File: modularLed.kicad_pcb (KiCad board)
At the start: 2 copper layers, 101.6 x 101.6 mm, 173 parts, among them IC101 ATMEGA328P-A, J101 POWER_JACKPTH, M301 FDS4935BZ, M302 FDS4935BZ, M303 FDS4935BZ, M304 FDS4935BZ, M305 FDS4935BZ, M306 FDS4935BZ, M307 FDS4935BZ, M308 FDS4935BZ, M401 FDS4935BZ, M402 FDS4935BZ, M403 FDS4935BZ, M404 FDS4935BZ, M405 FDS4935BZ, M406 FDS4935BZ, M407 FDS4935BZ, M408 FDS4935BZ, M501 FDS4935BZ, M502 FDS4935BZ, M503 FDS4935BZ, M504 FDS4935BZ, M505 FDS4935BZ, M506 FDS4935BZ, M507 FDS4935BZ, M508 FDS4935BZ, M601 FDS4935BZ, M602 FDS4935BZ, M603 FDS4935BZ, M604 FDS4935BZ, M605 FDS4935BZ, M606 FDS4935BZ, M607 FDS4935BZ, M608 FDS4935BZ, P101 CONN_01X04, P102 CONN_01X04, P103 CONN_01X04, P104 CONN_01X04, P105 CONN_01X06, P106 CONN_01X06, P107 CONN_01X06, P108 CONN_01X06, P109 CONN_02X03, P701 CONN_01X06, U101 ISL83485, U102 R-78E-0.5, U103 TLC5941, U104 74LS283, U105 74LS283, U201 74LS139, U301 74154, U401 74154, U501 74154, U601 74154, U701 ESP-12, U702 ISL83485

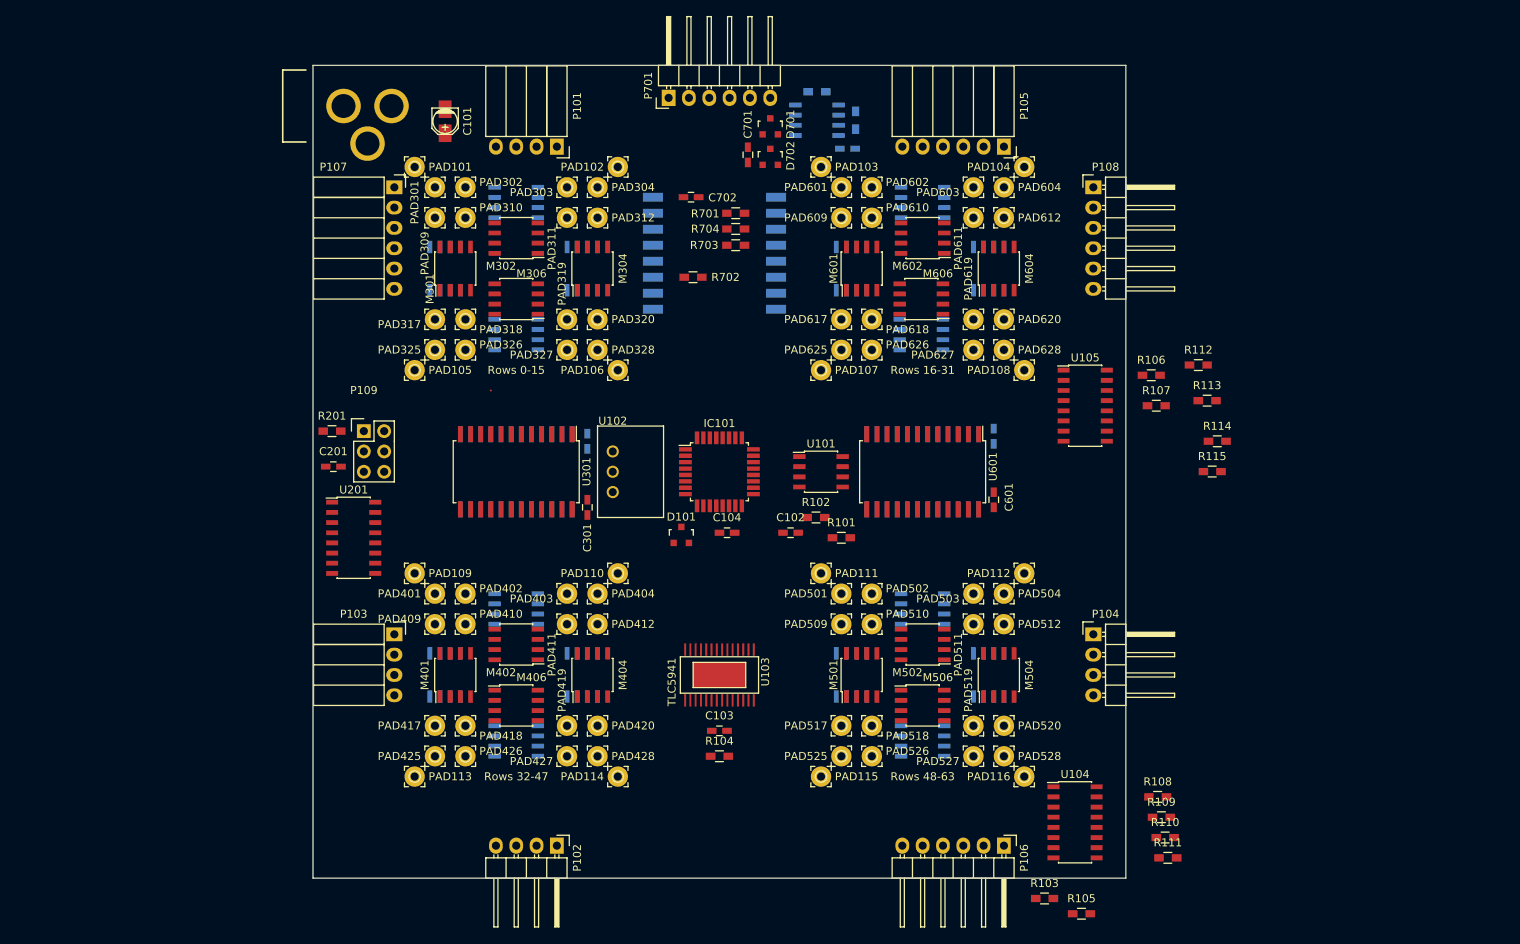
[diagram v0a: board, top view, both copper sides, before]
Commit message: Routed fet to row signals
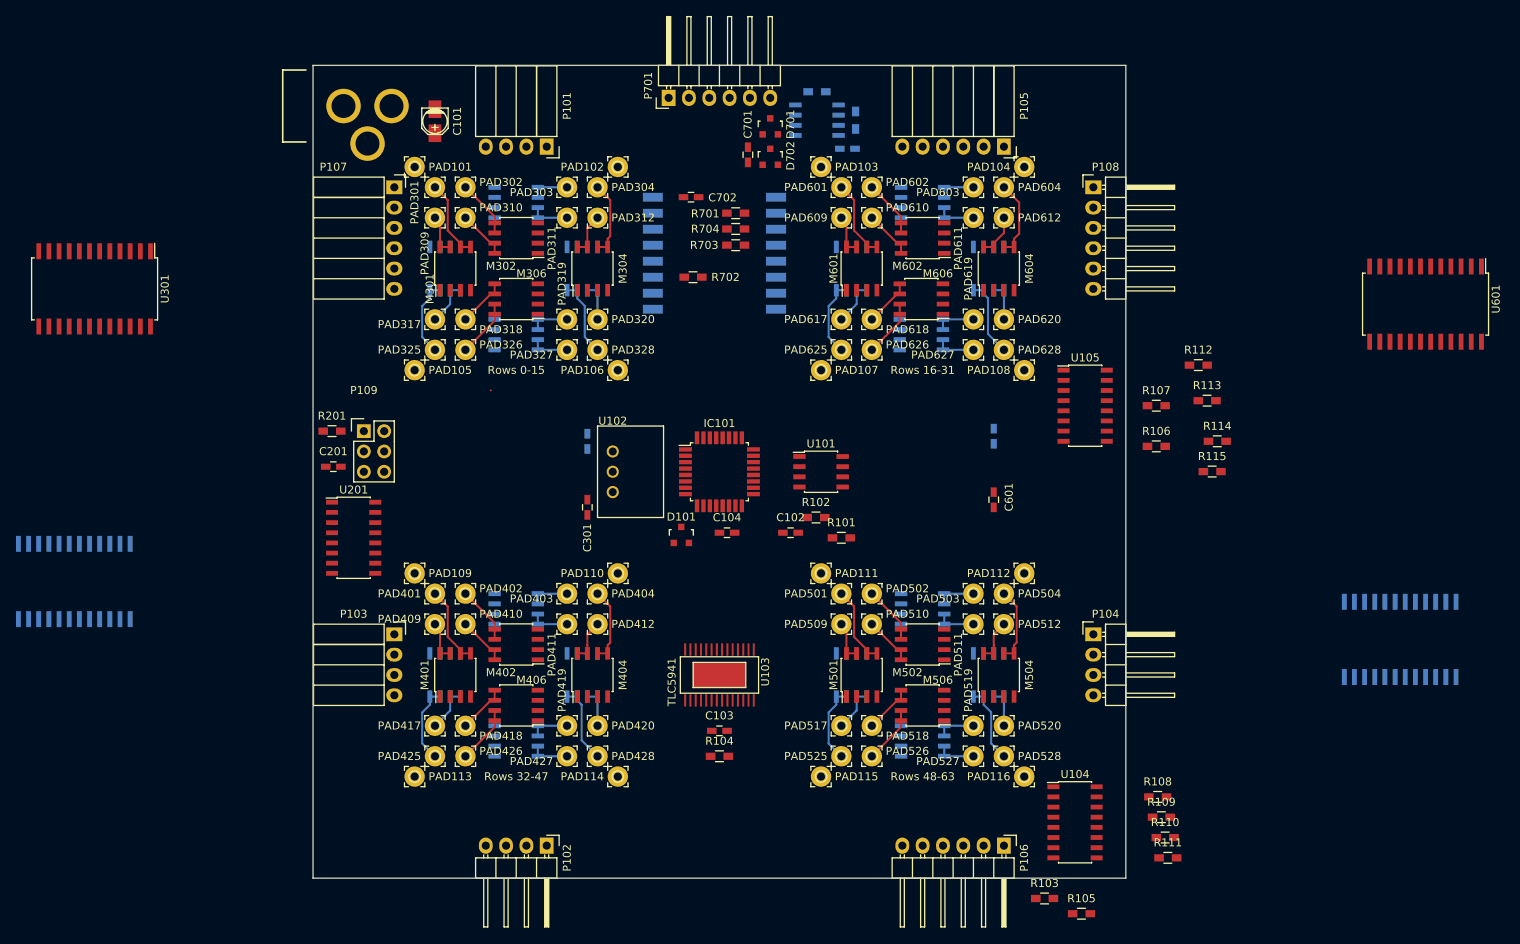
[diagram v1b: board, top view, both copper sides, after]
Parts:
- moved U601 66.3 mm to (228.0, 80.6)
- moved U501 63.3 mm to (224.8, 122.6)
- moved U301 57.4 mm to (61.6, 78.7)
- moved U401 56.9 mm to (59.1, 115.3)
- moved R106 8.91 mm to (194.3, 98.4)
- moved C101 1.27 mm to (104.1, 57.8)
- moved P101 1.27 mm to (118.1, 61.0)
- moved P102 1.27 mm to (118.1, 148.3)
- turned M406 to 180 degrees
- turned M506 to 180 degrees
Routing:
- net Net-(M401-Pad5): track 0.00 -> 10.0 mm
- net Net-(M301-Pad5): track 0.00 -> 10.0 mm
- net Net-(M601-Pad5): track 0.00 -> 10.0 mm
- net Net-(M501-Pad5): track 0.00 -> 10.0 mm
- net Net-(M405-Pad7): track 0.00 -> 9.79 mm
- net Net-(M305-Pad7): track 0.00 -> 9.79 mm
- net Net-(M505-Pad7): track 0.00 -> 9.79 mm
- net Net-(M605-Pad7): track 0.00 -> 9.79 mm
- net Net-(M508-Pad7): track 0.00 -> 9.78 mm
- net Net-(M604-Pad5): track 0.00 -> 9.78 mm
- net Net-(M408-Pad7): track 0.00 -> 9.78 mm
- net Net-(M608-Pad7): track 0.00 -> 9.78 mm
- net Net-(M308-Pad7): track 0.00 -> 9.78 mm
- net Net-(M404-Pad5): track 0.00 -> 9.53 mm
- net Net-(M304-Pad5): track 0.00 -> 9.53 mm
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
